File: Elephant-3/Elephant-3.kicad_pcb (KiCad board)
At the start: 2 copper layers, 90.2 x 58.4 mm, 61 parts, among them CON1 AVR-ISP-6, J1 7-25V, J10 Micro_SD_Card_Det, J11 IgnCap, J12 Main, J2 ADC2, J3 ADC1, J4 ADC0, J5 Switch, J6 18V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

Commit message: Finished ground on PCB and generated Gerber
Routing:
- net GND: track 0.00 -> 52.3 mm, vias 0 -> 15
- net +3V3: track 21.9 -> 26.6 mm
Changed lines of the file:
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@@
     (thickness 1.6)
     (drawings 4)
-    (tracks 431)
+    (tracks 487)
     (zones 0)
     (modules 61)
@@
       (drillshape 0)
       (scaleselection 1)
-      (outputdirectory /Users/corwin/Desktop/Elaphant-3-Gerber/))
+      (outputdirectory ../Gerber/))
   )
   (net 0 "")
@@
   (segment (start 138.43 100.33) (end 140.97 100.33) (width 0.5) (layer F.Cu) (net 1))
   (segment (start 148.59 105.41) (end 151.13 105.41) (width 0.5) (layer F.Cu) (net 1))
+  (segment (start 123.28 124.99) (end 123.676 124.99) (width 0.25) (layer F.Cu) (net 2))
+  (segment (start 123.676 124.99) (end 124.714 123.952) (width 0.25) (layer F.Cu) (net 2))
+  (via (at 124.714 123.952) (size 0.8) (drill 0.4) (layers F.Cu B.Cu) (net 2))
+  (segment (start 123.28 124.99) (end 123.28 123.28) (width 0.25) (layer F.Cu) (net 2))
+  (segment (start 123.28 123.28) (end 123.19 123.19) (width 0.25) (layer F.Cu) (net 2))
+  (via (at 123.19 123.19) (size 0.8) (drill 0.4) (layers F.Cu B.Cu) (net 2))
+  (segment (start 165.1 97.79) (end 158.75 97.79) (width 1) (layer B.Cu) (net 2))
+  (segment (start 170.815 104.97) (end 168.47 104.97) (width 0.25) (layer B.Cu) (net 2))
+  (segment (start 168.47 104.97) (end 165.1 101.6) (width 0.25) (layer B.Cu) (net 2))
+  (segment (start 165.1 101.6) (end 165.1 97.79) (width 0.25) (layer B.Cu) (net 2))
+  (segment (start 158.75 97.79) (end 157.48 97.79) (width 0.25) (layer B.Cu) (net 2))
+  (segment (start 157.48 97.79) (end 156.21 99.06) (width 0.25) (layer B.Cu) (net 2))
+  (segment (start 156.21 99.06) (end 152.4 99.06) (width 0.25) (layer B.Cu) (net 2))
+  (segment (start 152.4 99.06) (end 151.892 98.552) (width 0.25) (layer B.Cu) (net 2))
+  (segment (start 151.892 98.552) (end 151.892 95.123) (width 0.25) (layer B.Cu) (net 2))
+  (segment (start 110.888 114.19) (end 110.998 114.3) (width 0.25) (layer F.Cu) (net 2))
+  (segment (start 109.78 114.19) (end 110.888 114.19) (width 0.25) (layer F.Cu) (net 2))
+  (via (at 110.998 114.3) (size 0.8) (drill 0.4) (layers F.Cu B.Cu) (net 2))
+  (segment (start 110.53 114.19) (end 110.998 113.722) (width 0.25) (layer F.Cu) (net 2))
+  (segment (start 110.998 113.722) (end 110.998 113.411) (width 0.25) (layer F.Cu) (net 2))
+  (segment (start 109.78 114.19) (end 110.53 114.19) (width 0.25) (layer F.Cu) (net 2))
+  (via (at 110.998 113.411) (size 0.8) (drill 0.4) (layers F.Cu B.Cu) (net 2))
+  (segment (start 122.188 105.805) (end 122.174 105.791) (width 0.25) (layer F.Cu) (net 2))
+  (segment (start 124.054 105.805) (end 122.188 105.805) (width 0.25) (layer F.Cu) (net 2))
+  (via (at 122.174 105.791) (size 0.8) (drill 0.4) (layers F.Cu B.Cu) (net 2))
+  (segment (start 124.054 107.29) (end 124.079 107.315) (width 0.25) (layer F.Cu) (net 2))
+  (segment (start 124.054 105.805) (end 124.054 107.29) (width 0.25) (layer F.Cu) (net 2))
+  (via (at 124.079 107.315) (size 0.8) (drill 0.4) (layers F.Cu B.Cu) (net 2))
+  (segment (start 126.586 115.951) (end 125.094992 115.951) (width 0.25) (layer F.Cu) (net 2))
+  (via (at 125.094992 115.951) (size 0.8) (drill 0.4) (layers F.Cu B.Cu) (net 2))
+  (segment (start 126.586 115.951) (end 126.586 117.061004) (width 0.25) (layer F.Cu) (net 2))
+  (segment (start 126.586 117.061004) (end 126.618996 117.094) (width 0.25) (layer F.Cu) (net 2))
+  (via (at 126.618996 117.094) (size 0.8) (drill 0.4) (layers F.Cu B.Cu) (net 2))
+  (segment (start 109.78 124.54) (end 110.918 124.54) (width 0.25) (layer F.Cu) (net 2))
+  (segment (start 110.918 124.54) (end 110.998 124.46) (width 0.25) (layer F.Cu) (net 2))
+  (via (at 110.998 124.46) (size 0.8) (drill 0.4) (layers F.Cu B.Cu) (net 2))
+  (segment (start 109.78 124.54) (end 110.062 124.54) (width 0.25) (layer F.Cu) (net 2))
+  (segment (start 110.062 124.54) (end 110.998 125.476) (width 0.25) (layer F.Cu) (net 2))
+  (via (at 110.998 125.476) (size 0.8) (drill 0.4) (layers F.Cu B.Cu) (net 2))
+  (segment (start 113.88 111.212982) (end 113.919 111.251982) (width 0.25) (layer F.Cu) (net 2))
+  (segment (start 113.88 109.89) (end 113.88 111.212982) (width 0.25) (layer F.Cu) (net 2))
+  (via (at 113.919 111.251982) (size 0.8) (drill 0.4) (layers F.Cu B.Cu) (net 2))
+  (segment (start 120.93 109.89) (end 121.701 109.89) (width 0.25) (layer F.Cu) (net 2))
+  (segment (start 121.701 109.89) (end 122.174 110.363) (width 0.25) (layer F.Cu) (net 2))
+  (via (at 122.174 110.363) (size 0.8) (drill 0.4) (layers F.Cu B.Cu) (net 2))
+  (segment (start 120.93 109.89) (end 121.377 109.89) (width 0.25) (layer F.Cu) (net 2))
+  (segment (start 121.377 109.89) (end 122.174 109.093) (width 0.25) (layer F.Cu) (net 2))
+  (via (at 122.174 109.093) (size 0.8) (drill 0.4) (layers F.Cu B.Cu) (net 2))
+  (segment (start 109.78 124.54) (end 109.78 122.607) (width 0.25) (layer F.Cu) (net 2))
+  (segment (start 109.78 122.607) (end 109.347 122.174) (width 0.25) (layer F.Cu) (net 2))
+  (via (at 109.347 122.174) (size 0.8) (drill 0.4) (layers F.Cu B.Cu) (net 2))
+  (segment (start 113.88 109.89) (end 113.88 108.878) (width 0.25) (layer F.Cu) (net 2))
+  (segment (start 113.88 108.878) (end 114.173 108.585) (width 0.25) (layer F.Cu) (net 2))
+  (via (at 114.173 108.585) (size 0.8) (drill 0.4) (layers F.Cu B.Cu) (net 2))
   (segment (start 132.08 73.66) (end 132.08 80.01) (width 0.5) (layer F.Cu) (net 3) (status C00000))
   (segment (start 132.08 80.01) (end 132.715 80.645) (width 0.5) (layer F.Cu) (net 3) (status C00000))
@@
   (segment (start 136.525 114.1) (end 136.525 112.395) (width 0.25) (layer F.Cu) (net 8) (status 400000))
   (segment (start 136.525 112.395) (end 140.97 107.95) (width 0.25) (layer F.Cu) (net 8) (status 800000))
+  (segment (start 115.57 107.315) (end 115.57 105.689) (width 0.5) (layer F.Cu) (net 9))
+  (segment (start 115.57 105.689) (end 117.754 103.505) (width 0.5) (layer F.Cu) (net 9))
   (segment (start 124.054 103.505) (end 124.7525 104.2035) (width 0.5) (layer F.Cu) (net 9) (status C00000))
   (segment (start 124.7525 104.2035) (end 125.6665 104.2035) (width 0.5) (layer F.Cu) (net 9) (status 400000))
@@
     (connect_pads (clearance 0.508))
     (min_thickness 0.254)
-    (fill yes (arc_segments 16) (thermal_gap 0.508) (thermal_bridge_width 0.508))
+    (fill yes (arc_segments 16) (thermal_gap 0.508) (thermal_bridge_width 1))
     (polygon
       (pts
@@
     (connect_pads (clearance 0.508))
     (min_thickness 0.254)
-    (fill yes (arc_segments 16) (thermal_gap 0.508) (thermal_bridge_width 0.508))
+    (fill yes (arc_segments 16) (thermal_gap 0.508) (thermal_bridge_width 2))
     (polygon
       (pts

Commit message: Updated some tracks
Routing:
- net GND: track 52.3 -> 51.4 mm
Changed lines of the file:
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@@
     (thickness 1.6)
     (drawings 4)
-    (tracks 487)
+    (tracks 486)
     (zones 0)
     (modules 61)
@@
   (gr_line (start 107.95 127) (end 198.12 127) (layer Edge.Cuts) (width 0.15))
   (gr_line (start 107.95 68.58) (end 107.95 127) (layer Edge.Cuts) (width 0.15))
+  (segment (start 163.576 97.79) (end 158.75 97.79) (width 1) (layer B.Cu) (net 2))
+  (segment (start 170.815 104.97) (end 168.47 104.97) (width 0.25) (layer B.Cu) (net 2))
+  (segment (start 168.47 104.97) (end 163.576 100.076) (width 0.25) (layer B.Cu) (net 2))
+  (segment (start 163.576 100.076) (end 163.576 97.79) (width 0.25) (layer B.Cu) (net 2))
+  (segment (start 164.465 71.12) (end 164.465 90.297) (width 0.5) (layer F.Cu) (net 14))
+  (segment (start 166.751 97.409) (end 166.751 92.583) (width 0.5) (layer B.Cu) (net 14))
+  (segment (start 166.351001 92.183001) (end 166.751 92.583) (width 0.5) (layer F.Cu) (net 14))
+  (segment (start 164.465 90.297) (end 166.351001 92.183001) (width 0.5) (layer F.Cu) (net 14))
+  (via (at 166.751 92.583) (size 0.8) (drill 0.4) (layers F.Cu B.Cu) (net 14))
+  (segment (start 163.049999 101.109995) (end 166.351001 97.808993) (width 0.5) (layer F.Cu) (net 14))
+  (segment (start 163.049999 118.599999) (end 163.049999 101.109995) (width 0.5) (layer F.Cu) (net 14))
+  (segment (start 166.351001 97.808993) (end 166.751 97.408994) (width 0.5) (layer F.Cu) (net 14))
+  (segment (start 165.1 120.65) (end 163.049999 118.599999) (width 0.5) (layer F.Cu) (net 14))
+  (via (at 166.751 97.408994) (size 0.8) (drill 0.4) (layers F.Cu B.Cu) (net 14))
+  (segment (start 166.751 97.409) (end 166.751 97.408994) (width 0.5) (layer F.Cu) (net 14))
   (segment (start 138.43 100.33) (end 138.43 96.647) (width 0.5) (layer F.Cu) (net 1))
   (segment (start 138.43 96.647) (end 137.795 96.012) (width 0.5) (layer F.Cu) (net 1))
@@
   (segment (start 123.28 123.28) (end 123.19 123.19) (width 0.25) (layer F.Cu) (net 2))
   (via (at 123.19 123.19) (size 0.8) (drill 0.4) (layers F.Cu B.Cu) (net 2))
-  (segment (start 165.1 97.79) (end 158.75 97.79) (width 1) (layer B.Cu) (net 2))
-  (segment (start 170.815 104.97) (end 168.47 104.97) (width 0.25) (layer B.Cu) (net 2))
-  (segment (start 168.47 104.97) (end 165.1 101.6) (width 0.25) (layer B.Cu) (net 2))
-  (segment (start 165.1 101.6) (end 165.1 97.79) (width 0.25) (layer B.Cu) (net 2))
   (segment (start 158.75 97.79) (end 157.48 97.79) (width 0.25) (layer B.Cu) (net 2))
   (segment (start 157.48 97.79) (end 156.21 99.06) (width 0.25) (layer B.Cu) (net 2))
@@
   (segment (start 124.206 119.126) (end 133.477 119.126) (width 0.25) (layer F.Cu) (net 13))
   (segment (start 120.65 115.57) (end 124.206 119.126) (width 0.25) (layer F.Cu) (net 13))
-  (segment (start 166.996422 97.156) (end 163.049999 101.102423) (width 0.5) (layer F.Cu) (net 14))
-  (segment (start 163.049999 101.102423) (end 163.049999 109.505999) (width 0.5) (layer F.Cu) (net 14))
-  (segment (start 166.9415 93.105997) (end 166.9415 97.101078) (width 0.5) (layer B.Cu) (net 14))
-  (segment (start 166.9415 97.101078) (end 166.996422 97.156) (width 0.5) (layer B.Cu) (net 14))
-  (via (at 166.996422 97.156) (size 0.8) (drill 0.4) (layers F.Cu B.Cu) (net 14))
-  (segment (start 164.465 71.12) (end 164.465 72.322081) (width 0.5) (layer F.Cu) (net 14))
-  (via (at 166.9415 93.105997) (size 0.8) (drill 0.4) (layers F.Cu B.Cu) (net 14))
-  (segment (start 164.465 72.322081) (end 166.9415 74.798581) (width 0.5) (layer F.Cu) (net 14))
-  (segment (start 166.9415 74.798581) (end 166.9415 93.105997) (width 0.5) (layer F.Cu) (net 14))
-  (segment (start 165.1 120.65) (end 164.1475 119.6975) (width 0.5) (layer F.Cu) (net 14))
-  (segment (start 164.1475 119.6975) (end 164.1475 112.540001) (width 0.5) (layer F.Cu) (net 14))
-  (segment (start 164.1475 112.540001) (end 164.115999 112.540001) (width 0.5) (layer F.Cu) (net 14))
-  (segment (start 164.115999 112.540001) (end 163.049999 111.474001) (width 0.5) (layer F.Cu) (net 14))
-  (segment (start 163.049999 111.474001) (end 163.049999 109.505999) (width 0.5) (layer F.Cu) (net 14))
   (segment (start 155.575 125.095) (end 156.845 125.095) (width 0.5) (layer F.Cu) (net 14))
   (segment (start 156.845 125.095) (end 158.115 123.825) (width 0.5) (layer F.Cu) (net 14))
@@
   (segment (start 179.705 115.57) (end 180.721 116.586) (width 0.25) (layer F.Cu) (net 32))
   (segment (start 180.721 116.586) (end 184.15 116.586) (width 0.25) (layer F.Cu) (net 32))
+  (segment (start 154.44999 78.163986) (end 154.44999 79.605994) (width 0.25) (layer F.Cu) (net 33))
+  (segment (start 167.849315 95.631) (end 168.415 95.631) (width 0.25) (layer F.Cu) (net 33))
+  (segment (start 156.7815 81.937504) (end 156.7815 91.2495) (width 0.25) (layer F.Cu) (net 33))
+  (segment (start 167.594313 95.375998) (end 167.849315 95.631) (width 0.25) (layer F.Cu) (net 33))
+  (segment (start 154.44999 79.605994) (end 156.7815 81.937504) (width 0.25) (layer F.Cu) (net 33))
+  (segment (start 150.495 78.34) (end 151.62001 77.21499) (width 0.25) (layer F.Cu) (net 33))
+  (segment (start 153.500994 77.21499) (end 154.44999 78.163986) (width 0.25) (layer F.Cu) (net 33))
+  (segment (start 160.907998 95.375998) (end 167.594313 95.375998) (width 0.25) (layer F.Cu) (net 33))
+  (segment (start 150.495 78.74) (end 150.495 78.34) (width 0.25) (layer F.Cu) (net 33))
+  (segment (start 156.7815 91.2495) (end 160.907998 95.375998) (width 0.25) (layer F.Cu) (net 33))
+  (segment (start 151.62001 77.21499) (end 153.500994 77.21499) (width 0.25) (layer F.Cu) (net 33))
   (segment (start 173.215 95.631) (end 177.6095 95.631) (width 0.25) (layer F.Cu) (net 33))
   (segment (start 177.6095 95.631) (end 184.15 102.1715) (width 0.25) (layer F.Cu) (net 33))
   (segment (start 168.415 95.631) (end 173.215 95.631) (width 0.25) (layer B.Cu) (net 33))
   (via (at 173.215 95.631) (size 0.8) (drill 0.4) (layers F.Cu B.Cu) (net 33))
-  (segment (start 156.7815 91.2495) (end 161.163 95.631) (width 0.25) (layer F.Cu) (net 33))
-  (segment (start 161.163 95.631) (end 168.415 95.631) (width 0.25) (layer F.Cu) (net 33))
   (via (at 168.415 95.631) (size 0.8) (drill 0.4) (layers F.Cu B.Cu) (net 33))
-  (segment (start 156.7815 81.937504) (end 156.7815 91.2495) (width 0.25) (layer F.Cu) (net 33))
-  (segment (start 153.500994 77.21499) (end 154.44999 78.163986) (width 0.25) (layer F.Cu) (net 33))
-  (segment (start 154.44999 78.163986) (end 154.44999 79.605994) (width 0.25) (layer F.Cu) (net 33))
-  (segment (start 154.44999 79.605994) (end 156.7815 81.937504) (width 0.25) (layer F.Cu) (net 33))
-  (segment (start 151.62001 77.21499) (end 153.500994 77.21499) (width 0.25) (layer F.Cu) (net 33))
-  (segment (start 150.495 78.74) (end 150.495 78.34) (width 0.25) (layer F.Cu) (net 33))
-  (segment (start 150.495 78.34) (end 151.62001 77.21499) (width 0.25) (layer F.Cu) (net 33))
   (segment (start 184.15 107.315) (end 184.15 102.1715) (width 0.25) (layer F.Cu) (net 33))
   (segment (start 179.705 110.49) (end 181.975 110.49) (width 0.25) (layer F.Cu) (net 33))

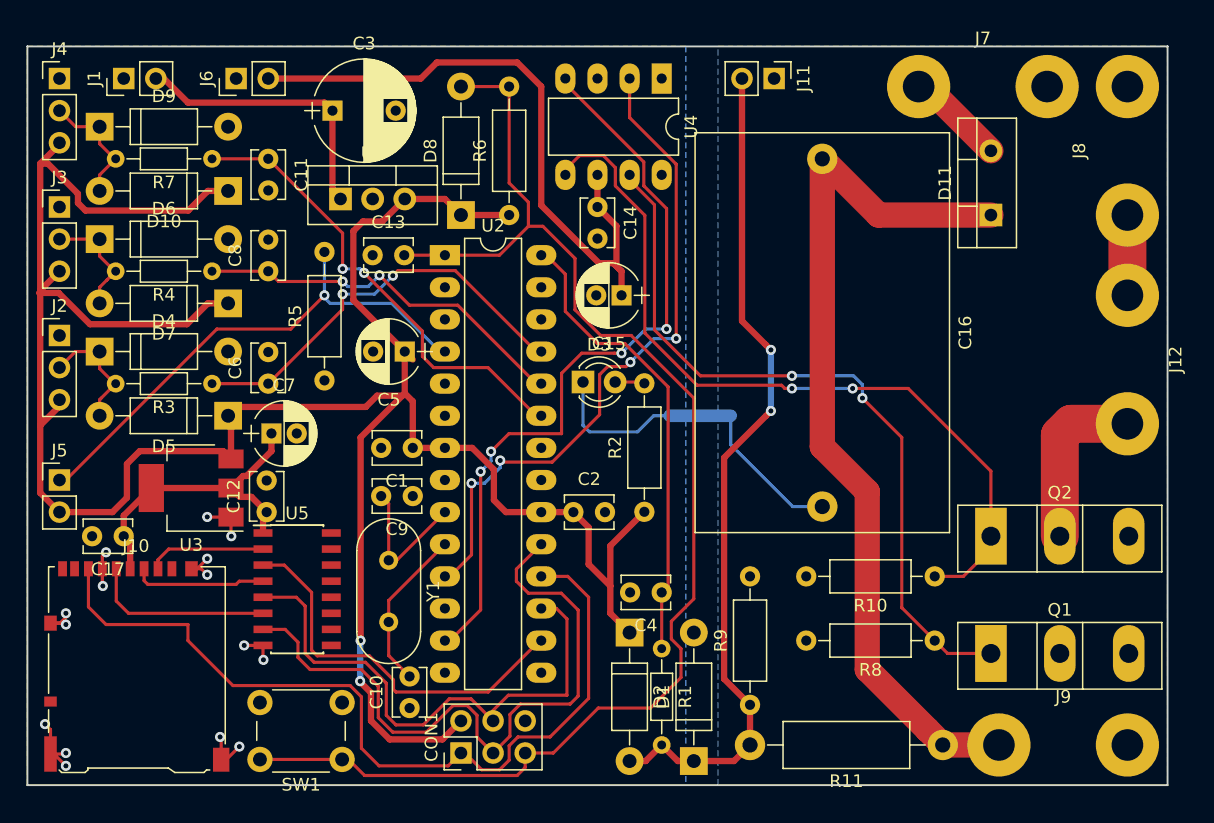
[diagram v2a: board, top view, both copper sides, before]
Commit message: Fixed some circuit mistakes
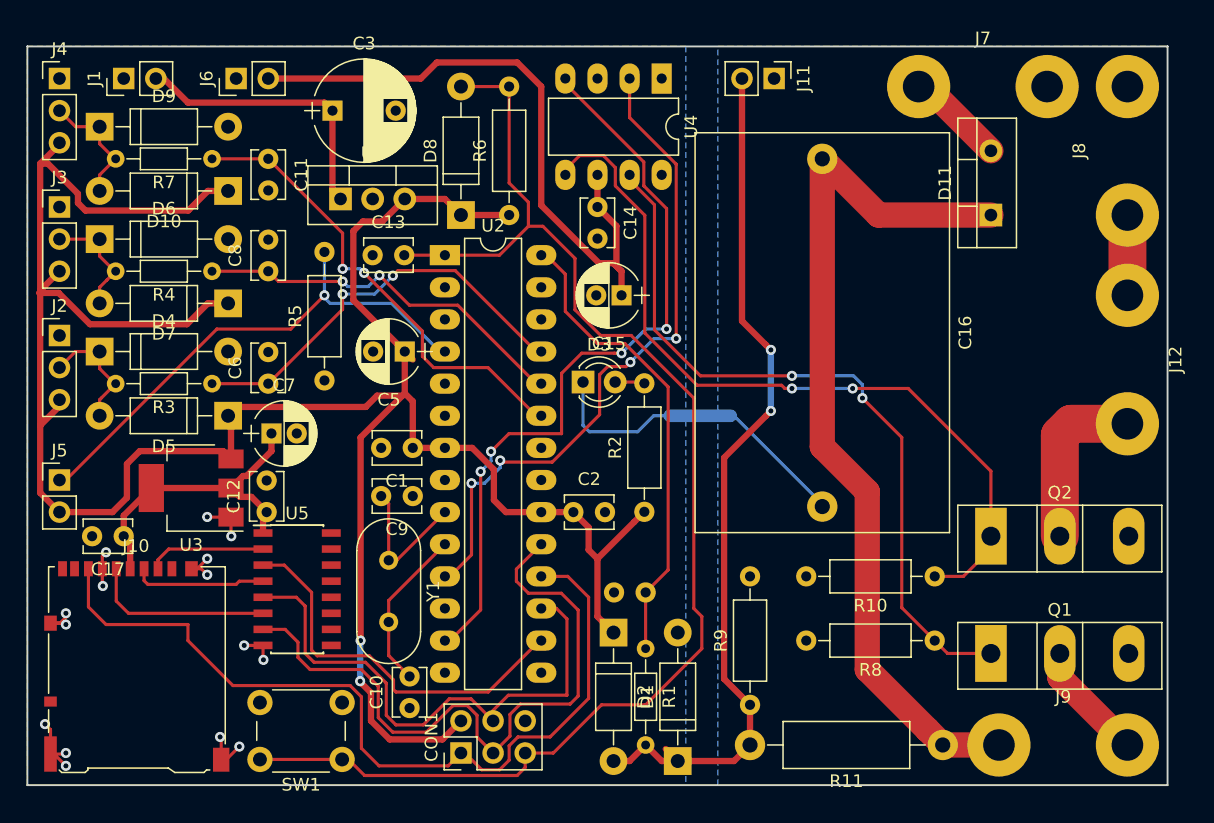
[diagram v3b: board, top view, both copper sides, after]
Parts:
- C4: moved to B.Cu
- moved C4 1.27 mm to (156.8, 111.8)
- moved D1 1.27 mm to (159.4, 125.1)
- moved R1 1.27 mm to (156.8, 116.2)
- moved D2 1.27 mm to (154.3, 114.9)
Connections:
- J10 pad 1: Net-(J10-Pad1) -> (no net)
- J10 pad 10: Net-(J10-Pad10) -> (no net)
- J10 pad 8: Net-(J10-Pad8) -> (no net)
- J10 pad 9: Net-(J10-Pad9) -> (no net)
- U2 pad 12: Net-(U2-Pad12) -> (no net)
- U2 pad 14: Net-(U2-Pad14) -> (no net)
- U2 pad 15: Net-(U2-Pad15) -> (no net)
- U2 pad 2: Net-(U2-Pad2) -> (no net)
- U2 pad 21: Net-(U2-Pad21) -> (no net)
- U2 pad 26: Net-(U2-Pad26) -> (no net)
- U2 pad 27: Net-(U2-Pad27) -> (no net)
- U2 pad 3: Net-(U2-Pad3) -> (no net)
- U2 pad 5: Net-(U2-Pad5) -> (no net)
- U2 pad 6: Net-(U2-Pad6) -> (no net)
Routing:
- net Net-(J9-Pad1): track 0.00 -> 9.45 mm
- net IgnCap: track 67.1 -> 69.8 mm
- net +5V: track 209.9 -> 207.7 mm
- net GND: track 51.4 -> 50.1 mm
- net Net-(C4-Pad1): track 37.0 -> 37.5 mm

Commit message: Labeled stuff on PCB
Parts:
- C4: moved to F.Cu
- CON1: value AVR-ISP-6 -> ISP
- J10: value Micro_SD_Card_Det -> Micro_SD_Card
- U1: value LM7805_TO220 -> LM7805
- U2: value ATMEGA328P-PU -> ATMEGA328
- U3: value LT1117-3.3 -> LT1117
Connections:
- J10 pad 1: (no net) -> Net-(J10-Pad1)
- J10 pad 10: (no net) -> Net-(J10-Pad10)
- J10 pad 8: (no net) -> Net-(J10-Pad8)
- J10 pad 9: (no net) -> Net-(J10-Pad9)
- U2 pad 12: (no net) -> Net-(U2-Pad12)
- U2 pad 14: (no net) -> Net-(U2-Pad14)
- U2 pad 15: (no net) -> Net-(U2-Pad15)
- U2 pad 2: (no net) -> Net-(U2-Pad2)
- U2 pad 21: (no net) -> Net-(U2-Pad21)
- U2 pad 26: (no net) -> Net-(U2-Pad26)
- U2 pad 27: (no net) -> Net-(U2-Pad27)
- U2 pad 3: (no net) -> Net-(U2-Pad3)
- U2 pad 5: (no net) -> Net-(U2-Pad5)
- U2 pad 6: (no net) -> Net-(U2-Pad6)
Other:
- board text added: "+"
- board text added: "+5V"
- board text added: "-"
- board text added: "GND"
